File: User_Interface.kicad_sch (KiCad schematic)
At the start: 0 parts

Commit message: wip
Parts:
- added Q4: MMBT2222A, Package_TO_SOT_SMD:SOT-23, symbol Transistor_BJT:MMBT2222A
- added R24: 100k, Resistor_SMD:R_0805_2012Metric, symbol Device:R
- added R25: 1k, Resistor_SMD:R_0805_2012Metric, symbol Device:R
- added SW2: Estop, symbol Switch:SW_Push_Open
- added SW3: SW_Push, symbol Switch:SW_Push
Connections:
- new net: Q4.1 (B), R24.2, SW2.1 (A)
- new net +3.3V: R24.1, R25.1
- new net Estop: Q4.3 (C), R25.2
- new net GNDD: Q4.2 (E), SW2.2 (B)
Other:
- note added: "Estop"
- note added: "Shoud it trigger driver and stm brake at once?"

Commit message: 90% schematic first layout
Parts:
- added C23, C24: 1u, Capacitor_SMD:C_0805_2012Metric_Pad1.18x1.45mm_HandSolder, symbol Device:C
- added Q2, Q3, Q5: BSS138, Package_TO_SOT_SMD:SOT-23, symbol Transistor_FET:BSS138
- added R20, R21, R22, R27, R29: 100k, Resistor_SMD:R_0805_2012Metric, symbol Device:R
- added R23, R26, R28: 1k, Resistor_SMD:R_0805_2012Metric, symbol Device:R
- added SW4: SW_Push, Button_Switch_THT:SW_PUSH_6mm_H5mm, symbol Switch:SW_Push
- R25: value 1k -> 10k
- SW3: footprint (none) -> Button_Switch_THT:SW_PUSH_6mm_H5mm
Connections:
- net +3.3V: now also R20.1, R21.1
- net GNDD: now also SW3.1, C23.2, C24.2, Q2.2 (S), Q3.2 (S), Q5.2 (S), R22.2, R27.2, R29.2, SW4.1
- net ESTOP: now reaches Q4.1 (B), R24.2, SW2.1 (A)
- net RUN/STOP: now reaches SW3.2
- net RUN/STOP: now also C23.1, R20.2
- new net: Q3.1 (G), R26.2, R27.1
- new net: Q5.1 (G), R28.2, R29.1
- new net: Q2.1 (G), R22.1, R23.2
- new net ERROR_LED: R23.1
- new net ERROR_LED-: Q2.3 (D)
- new net ESTOP_LED: R28.1
- new net ESTOP_LED-: Q5.3 (D)
- new net Error_Fixed: C24.1, R21.2, SW4.2
- new net RUN_LED: R26.1
- new net RUN_LED-: Q3.3 (D)
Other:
- note added: "Control light switches"
- note added: "Error fixed button"
- note added: "Run/Stop button"
- note removed: "Przyciski: ESTOP Run/Stop Error fixed Lampki: ESTOP ON RUN ERROR"
- moved on the sheet: Q4, R24, R25, SW2

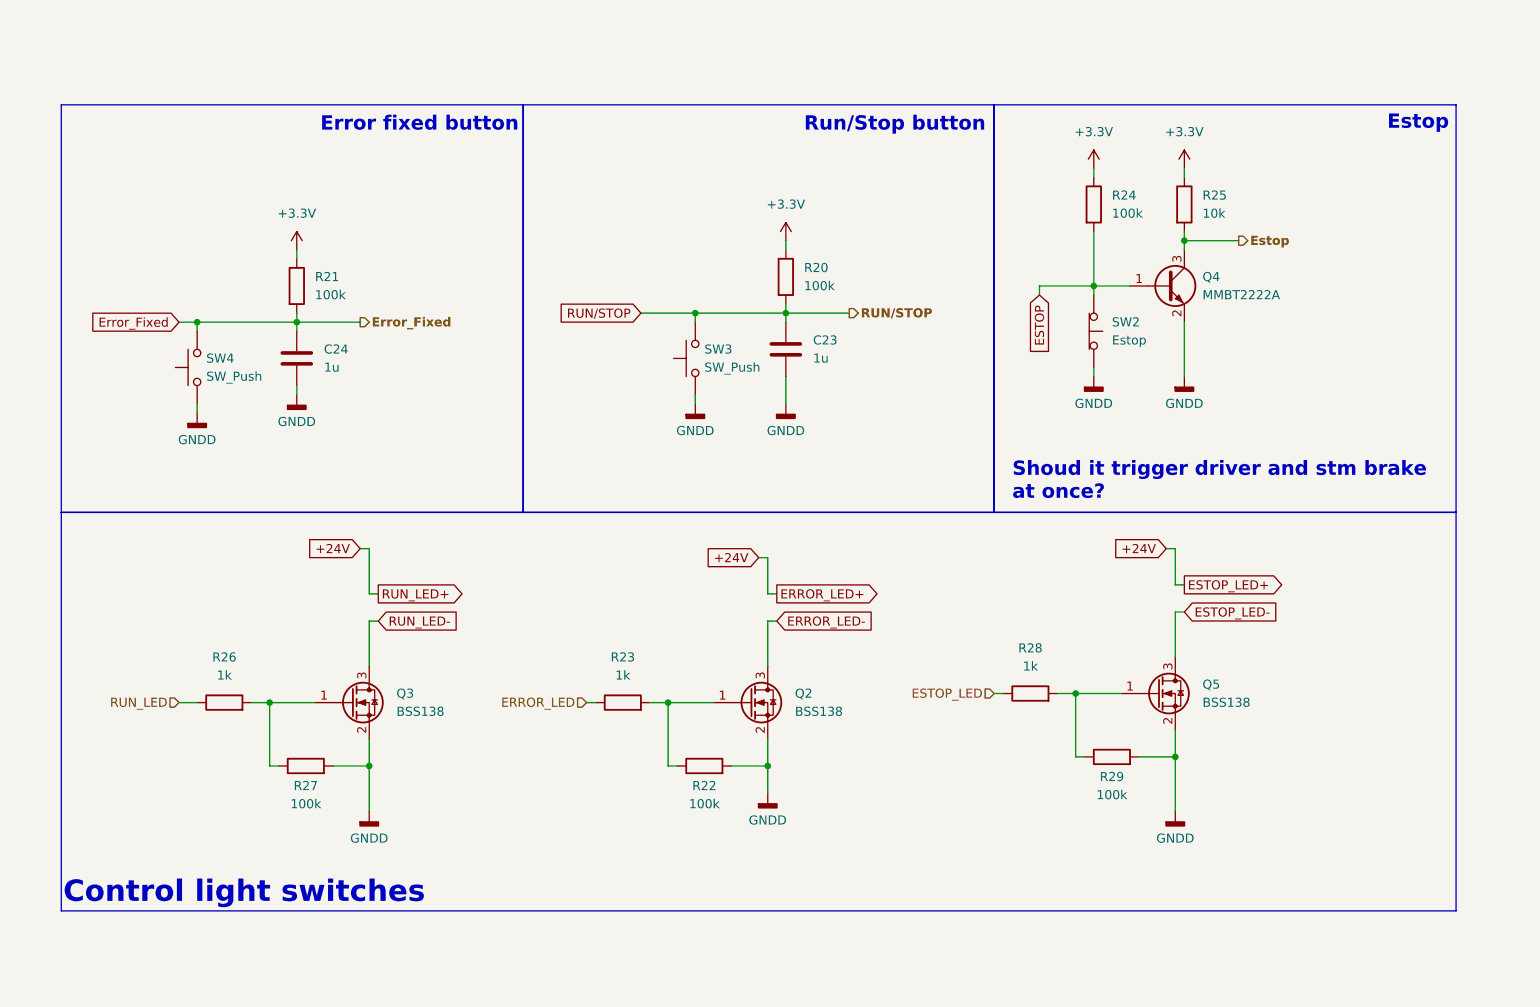
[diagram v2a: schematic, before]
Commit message: Addition of testpoints
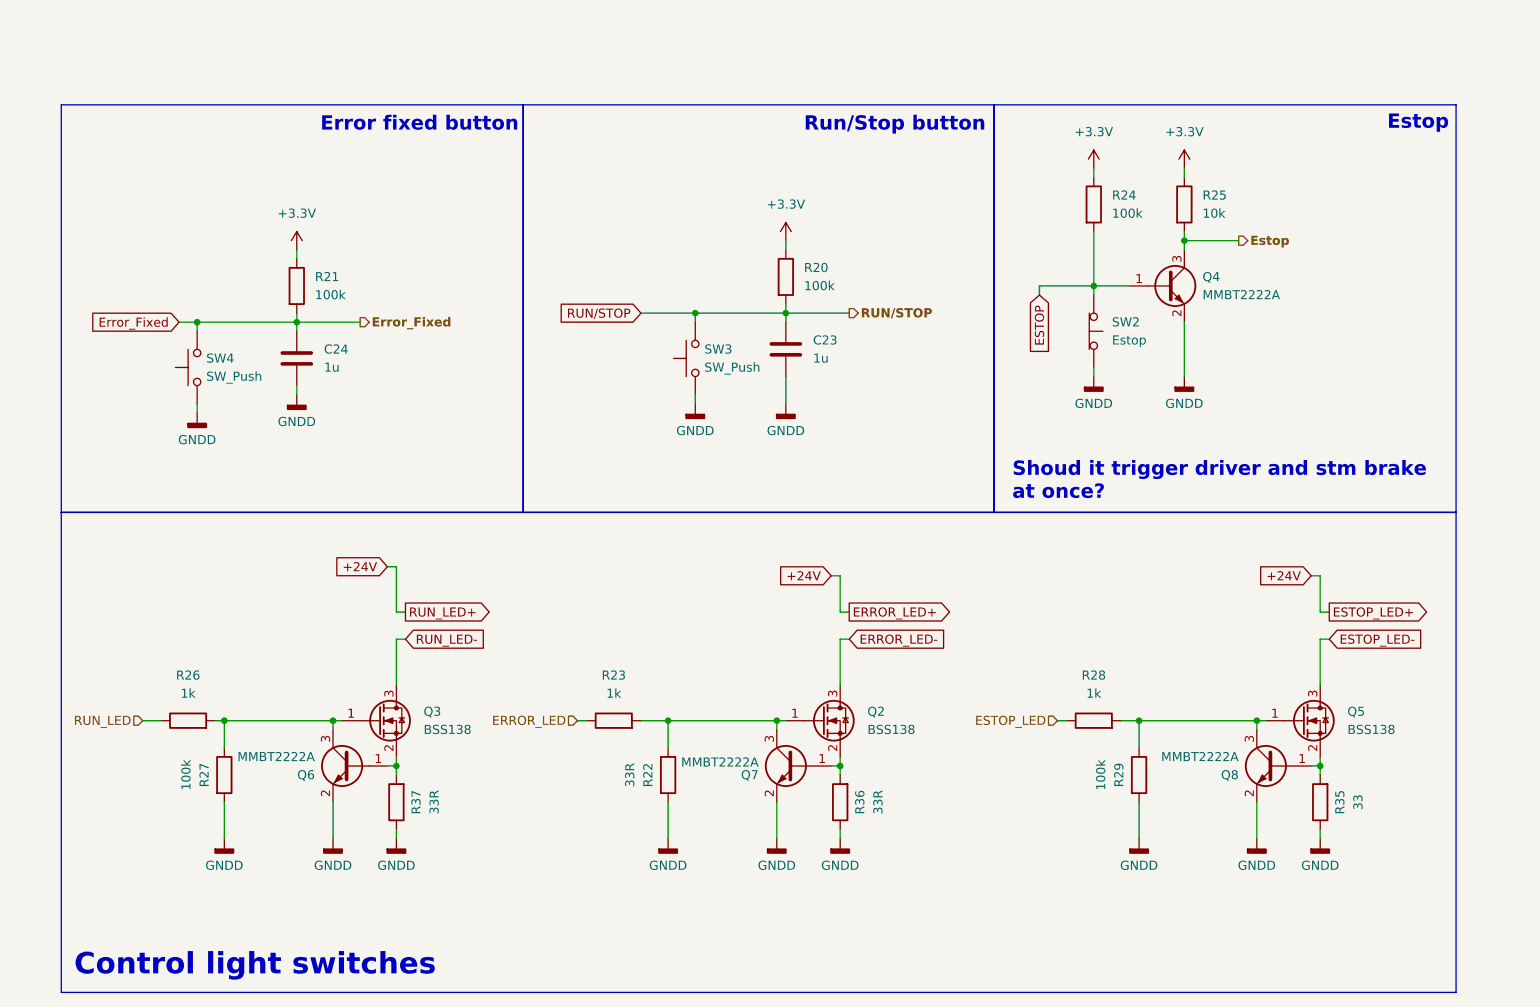
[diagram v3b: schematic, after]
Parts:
- added Q6, Q7, Q8: MMBT2222A, Package_TO_SOT_SMD:SOT-23, symbol Transistor_BJT:MMBT2222A
- added R35: 33, Resistor_SMD:R_0805_2012Metric, symbol Device:R
- added R36, R37: 33R, Resistor_SMD:R_0805_2012Metric, symbol Device:R
- R22: value 100k -> 33R
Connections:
- net GNDD: now also Q6.2 (E), Q7.2 (E), Q8.2 (E), R35.1, R36.1, R37.1; no longer Q2.2 (S), Q3.2 (S), Q5.2 (S)
- net at Q3.1 (G), R26.2, R27.1: now also Q6.3 (C)
- net at Q5.1 (G), R28.2, R29.1: now also Q8.3 (C)
- net at Q2.1 (G), R22.1, R23.2: now also Q7.3 (C)
- new net: Q2.2 (S), Q7.1 (B), R36.2
- new net: Q5.2 (S), Q8.1 (B), R35.2
- new net: Q3.2 (S), Q6.1 (B), R37.2
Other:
- moved on the sheet: Q2, Q3, Q5, R22, R23, R26, R27, R28, R29
